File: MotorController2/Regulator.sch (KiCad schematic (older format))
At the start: 21 parts, among them U4 IFX91041EJV50, U5 TC2117-3.3V

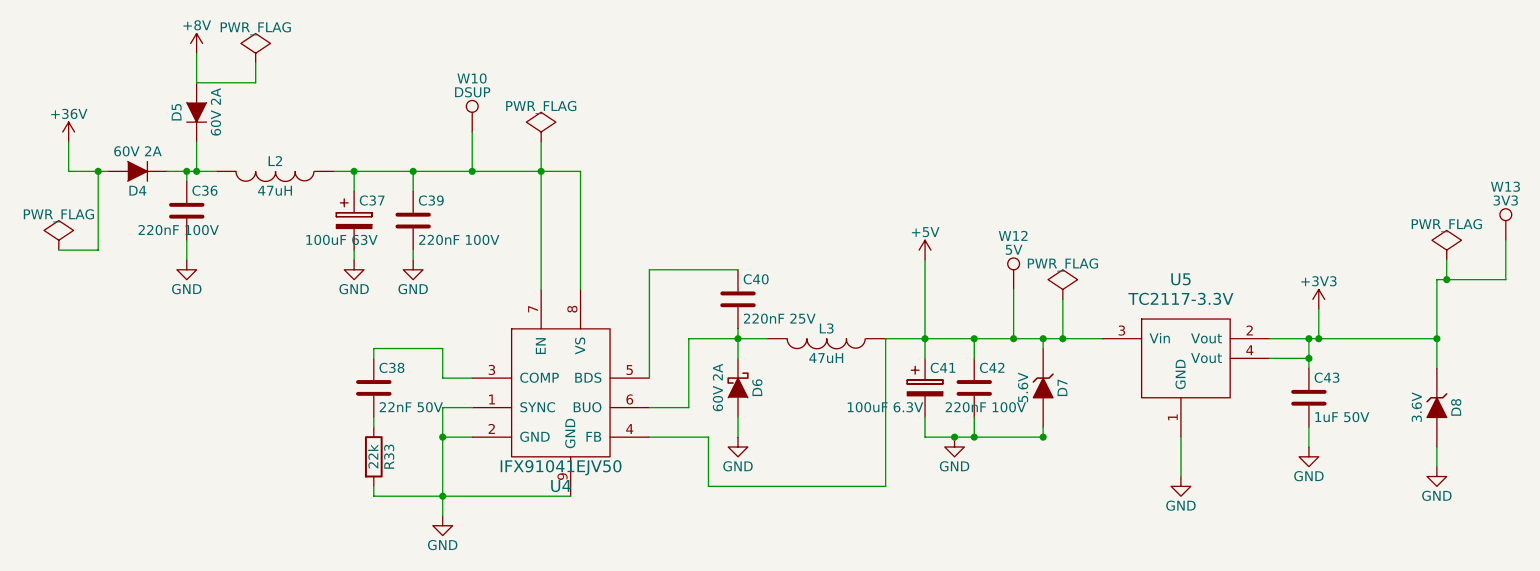
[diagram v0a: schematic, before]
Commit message: Add power off option.
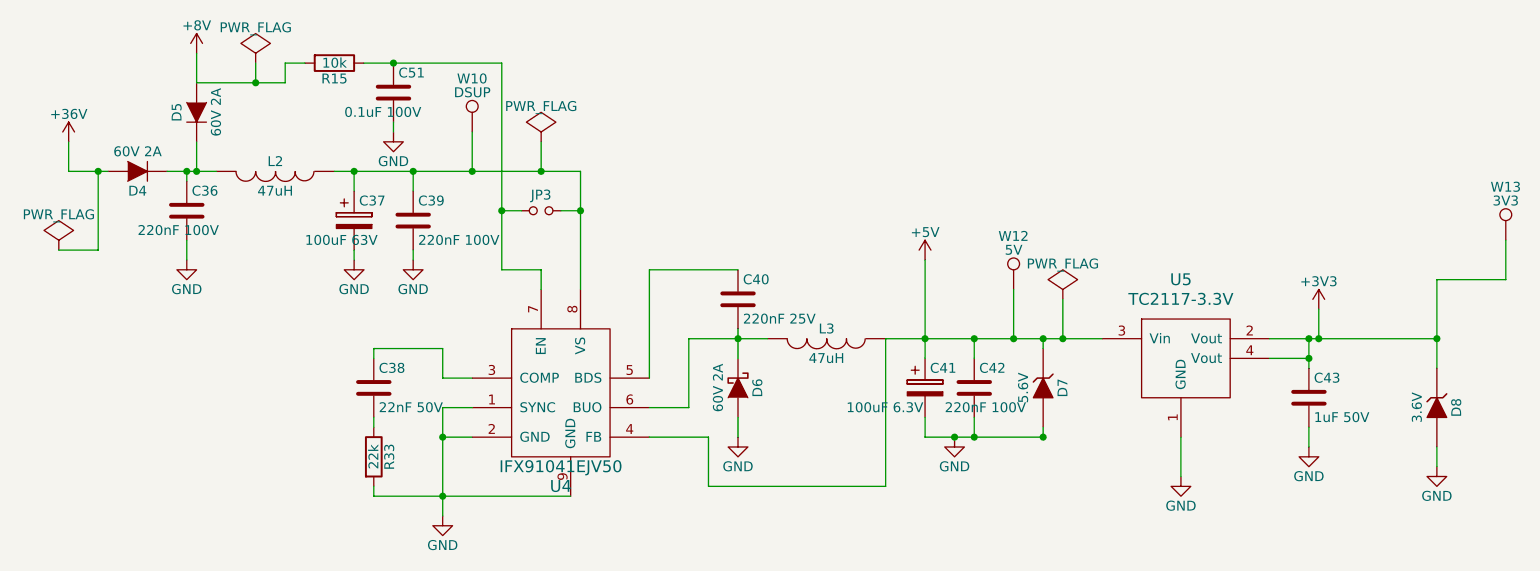
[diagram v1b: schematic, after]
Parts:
- added C51: 0.1uF 100V, Capacitors_SMD:C_0805_HandSoldering, symbol C
- added JP3: Jumper_NO_Small, Resistors_SMD:R_0805_HandSoldering, symbol Jumper_NO_Small
- added R15: 10k, Resistors_SMD:R_0805_HandSoldering, symbol R
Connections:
- net +8V: now also R15.2
- net GND: now also C51.2
- net at C37.1, C39.1, L2.1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: now also JP3.2; no longer U4.7 (EN)
- new net: C51.1, JP3.1, R15.1, U4.7 (EN)
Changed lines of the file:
@@
-EESchema Schematic File Version 3
+EESchema Schematic File Version 2
 LIBS:BMC2-rescue
 LIBS:power
@@
 LIBS:MIC2009A-1YM6TR
 LIBS:BMC2-cache
-EELAYER 26 0
+EELAYER 25 0
 EELAYER END
 $Descr A4 11693 8268
@@
 $EndDescr
 $Comp
-L GND #PWR077
+L GND #PWR053
 U 1 1 585F6F4B
 P 2850 3350
-F 0 "#PWR077" H 2850 3100 50  0001 C CNN
+F 0 "#PWR053" H 2850 3100 50  0001 C CNN
 F 1 "GND" H 2850 3200 50  0000 C CNN
 F 2 "" H 2850 3350 50  0000 C CNN
@@
 	2850 2650 3000 2650
 $Comp
-L +36V #PWR078
+L +36V #PWR054
 U 1 1 585F700E
 P 950 1450
-F 0 "#PWR078" H 950 1300 50  0001 C CNN
+F 0 "#PWR054" H 950 1300 50  0001 C CNN
 F 1 "+36V" H 950 1590 50  0000 C CNN
 F 2 "" H 950 1450 50  0000 C CNN
@@
 	4100 2800 4100 2450
 $Comp
-L GND #PWR079
+L GND #PWR055
 U 1 1 585F787D
 P 4350 2950
-F 0 "#PWR079" H 4350 2700 50  0001 C CNN
+F 0 "#PWR055" H 4350 2700 50  0001 C CNN
 F 1 "GND" H 4350 2800 50  0000 C CNN
 F 2 "" H 4350 2950 50  0000 C CNN
@@
 	4350 2950 4350 2850
 $Comp
-L GND #PWR080
+L GND #PWR056
 U 1 1 585F7983
 P 5450 2950
-F 0 "#PWR080" H 5450 2700 50  0001 C CNN
+F 0 "#PWR056" H 5450 2700 50  0001 C CNN
 F 1 "GND" H 5450 2800 50  0000 C CNN
 F 2 "" H 5450 2950 50  0000 C CNN
@@
 Connection ~ 2700 1600
 $Comp
-L GND #PWR081
+L GND #PWR057
 U 1 1 585F7C36
 P 1550 2050
-F 0 "#PWR081" H 1550 1800 50  0001 C CNN
+F 0 "#PWR057" H 1550 1800 50  0001 C CNN
 F 1 "GND" H 1550 1900 50  0000 C CNN
 F 2 "" H 1550 2050 50  0000 C CNN
@@
 $EndComp
 $Comp
-L GND #PWR082
+L GND #PWR058
 U 1 1 585F7C68
 P 2400 2050
-F 0 "#PWR082" H 2400 1800 50  0001 C CNN
+F 0 "#PWR058" H 2400 1800 50  0001 C CNN
 F 1 "GND" H 2400 1900 50  0000 C CNN
 F 2 "" H 2400 2050 50  0000 C CNN
@@
 $EndComp
 $Comp
-L GND #PWR083
+L GND #PWR059
 U 1 1 585F7C9A
 P 2700 2050
-F 0 "#PWR083" H 2700 1800 50  0001 C CNN
+F 0 "#PWR059" H 2700 1800 50  0001 C CNN
 F 1 "GND" H 2700 1900 50  0000 C CNN
 F 2 "" H 2700 2050 50  0000 C CNN
@@
 	2700 2050 2700 2000
 Wire Wire Line
-	3350 1450 3350 2200
+	3350 1450 3350 1600
 Connection ~ 3350 1600
 $Comp
@@
 $EndComp
 $Comp
-L +5V #PWR084
+L +5V #PWR060
 U 1 1 586591BB
 P 5300 2050
-F 0 "#PWR084" H 5300 1900 50  0001 C CNN
+F 0 "#PWR060" H 5300 1900 50  0001 C CNN
 F 1 "+5V" H 5300 2190 50  0000 C CNN
 F 2 "" H 5300 2050 50  0000 C CNN
@@
 Connection ~ 1600 1600
 $Comp
-L +8V #PWR085
+L +8V #PWR061
 U 1 1 5865931B
 P 1600 1000
-F 0 "#PWR085" H 1600 850 50  0001 C CNN
+F 0 "#PWR061" H 1600 850 50  0001 C CNN
 F 1 "+8V" H 1600 1140 50  0000 C CNN
 F 2 "" H 1600 1000 50  0000 C CNN
@@
 	1600 1000 1600 1150
 $Comp
-L GND #PWR086
+L GND #PWR062
 U 1 1 586595C6
 P 6600 3150
-F 0 "#PWR086" H 6600 2900 50  0001 C CNN
+F 0 "#PWR062" H 6600 2900 50  0001 C CNN
 F 1 "GND" H 6600 3000 50  0000 C CNN
 F 2 "" H 6600 3150 50  0000 C CNN
@@
 	6600 3150 6600 2950
 $Comp
-L +3V3 #PWR087
+L +3V3 #PWR063
 U 1 1 58659680
 P 7300 2300
-F 0 "#PWR087" H 7300 2150 50  0001 C CNN
+F 0 "#PWR063" H 7300 2150 50  0001 C CNN
 F 1 "+3V3" H 7300 2440 50  0000 C CNN
 F 2 "" H 7300 2300 50  0000 C CNN
@@
 $EndComp
 $Comp
-L GND #PWR088
+L GND #PWR064
 U 1 1 586598C9
 P 7250 3000
-F 0 "#PWR088" H 7250 2750 50  0001 C CNN
+F 0 "#PWR064" H 7250 2750 50  0001 C CNN
 F 1 "GND" H 7250 2850 50  0000 C CNN
 F 2 "" H 7250 3000 50  0000 C CNN
@@
 	7250 3000 7250 2900
 Wire Wire Line
-	7250 2600 7250 2450
+	7250 2450 7250 2600
 Connection ~ 7250 2450
 $Comp
@@
 	5300 2950 5900 2950
 $Comp
-L GND #PWR089
+L GND #PWR065
 U 1 1 5865A3E7
 P 7900 3100
-F 0 "#PWR089" H 7900 2850 50  0001 C CNN
+F 0 "#PWR065" H 7900 2850 50  0001 C CNN
 F 1 "GND" H 7900 2950 50  0000 C CNN
 F 2 "" H 7900 3100 50  0000 C CNN
@@
 Connection ~ 3000 1600
 $Comp
-L PWR_FLAG #FLG092
+L PWR_FLAG #FLG066
 U 1 1 5874647E
 P 6000 2250
-F 0 "#FLG092" H 6000 2345 50  0001 C CNN
+F 0 "#FLG066" H 6000 2345 50  0001 C CNN
 F 1 "PWR_FLAG" H 6000 2430 50  0000 C CNN
 F 2 "" H 6000 2250 50  0000 C CNN
@@
 Connection ~ 6000 2450
 $Comp
-L PWR_FLAG #FLG093
-U 1 1 58746589
-P 7950 2050
-F 0 "#FLG093" H 7950 2145 50  0001 C CNN
-F 1 "PWR_FLAG" H 7950 2230 50  0000 C CNN
-F 2 "" H 7950 2050 50  0000 C CNN
-F 3 "" H 7950 2050 50  0000 C CNN
-	1    7950 2050
-	1    0    0    -1
-$EndComp
-Wire Wire Line
-	7950 2050 7950 2150
-Connection ~ 7950 2150
-$Comp
-L PWR_FLAG #FLG094
+L PWR_FLAG #FLG067
 U 1 1 58746947
 P 1900 1050
-F 0 "#FLG094" H 1900 1145 50  0001 C CNN
+F 0 "#FLG067" H 1900 1145 50  0001 C CNN
 F 1 "PWR_FLAG" H 1900 1230 50  0000 C CNN
 F 2 "" H 1900 1050 50  0000 C CNN
@@
 	1900 1050 1900 1150
 Wire Wire Line
-	1900 1150 1600 1150
-$Comp
-L PWR_FLAG #FLG095
+	1600 1150 2050 1150
+$Comp
+L PWR_FLAG #FLG068
 U 1 1 58746A06
 P 900 2000
-F 0 "#FLG095" H 900 2095 50  0001 C CNN
+F 0 "#FLG068" H 900 2095 50  0001 C CNN
 F 1 "PWR_FLAG" H 900 2180 50  0000 C CNN
 F 2 "" H 900 2000 50  0000 C CNN
@@
 Connection ~ 1100 1600
 $Comp
-L PWR_FLAG #FLG096
+L PWR_FLAG #FLG069
 U 1 1 58764812
 P 3350 1450
-F 0 "#FLG096" H 3350 1545 50  0001 C CNN
+F 0 "#FLG069" H 3350 1545 50  0001 C CNN
 F 1 "PWR_FLAG" H 3350 1630 50  0000 C CNN
 F 2 "" H 3350 1450 50  0000 C CNN
@@
 $EndComp
 Connection ~ 7250 2550
-Wire Wire Line
-	7900 2150 8250 2150
 $Comp
 L TC2117-3.3V U5
@@
 Wire Wire Line
 	7050 2550 7250 2550
+$Comp
+L R R15
+U 1 1 59C4B75A
+P 2300 1050
+F 0 "R15" V 2380 1050 50  0000 C CNN
+F 1 "10k" V 2300 1050 50  0000 C CNN
+F 2 "Resistors_SMD:R_0805_HandSoldering" V 2230 1050 50  0001 C CNN
+F 3 "" H 2300 1050 50  0000 C CNN
+	1    2300 1050
+	0    1    1    0
+$EndComp
+$Comp
+L C C51
+U 1 1 59C4B98C
+P 2600 1200
+F 0 "C51" H 2625 1300 50  0000 L CNN
+F 1 "0.1uF 100V" H 2350 1100 50  0000 L CNN
+F 2 "Capacitors_SMD:C_0805_HandSoldering" H 2638 1050 50  0001 C CNN
+F 3 "" H 2600 1200 50  0000 C CNN
+F 4 "1856615" H 2600 1200 60  0001 C CNN "Farnell"
+	1    2600 1200
+	1    0    0    -1
+$EndComp
+Wire Wire Line
+	2050 1150 2050 1050
+Wire Wire Line
+	2050 1050 2150 1050
+Connection ~ 1900 1150
+Wire Wire Line
+	2450 1050 3150 1050
+$Comp
+L GND #PWR070
+U 1 1 59C4BBA7
+P 2600 1400
+F 0 "#PWR070" H 2600 1150 50  0001 C CNN
+F 1 "GND" H 2600 1250 50  0000 C CNN
+F 2 "" H 2600 1400 50  0000 C CNN
+F 3 "" H 2600 1400 50  0000 C CNN
+	1    2600 1400
+	1    0    0    -1
+$EndComp
+Wire Wire Line
+	2600 1400 2600 1350
+Wire Wire Line
+	3150 1050 3150 2100
+Wire Wire Line
+	3150 2100 3350 2100
+Wire Wire Line
+	3350 2100 3350 2200
+Connection ~ 2600 1050
+$Comp
+L Jumper_NO_Small JP3
+U 1 1 59C4C18F
+P 3350 1800
+F 0 "JP3" H 3350 1880 50  0000 C CNN
+F 1 "Jumper_NO_Small" H 3360 1740 50  0001 C CNN
+F 2 "Resistors_SMD:R_0805_HandSoldering" H 3350 1800 50  0001 C CNN
+F 3 "" H 3350 1800 50  0000 C CNN
+	1    3350 1800
+	1    0    0    -1
+$EndComp
+Wire Wire Line
+	3450 1800 3550 1800
+Connection ~ 3550 1800
+Wire Wire Line
+	3250 1800 3150 1800
+Connection ~ 3150 1800
+Wire Wire Line
+	7900 2150 8250 2150
 $EndSCHEMATC

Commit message: Updates for parts list.
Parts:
- C36, C40, C42: Price (none) -> 0.205
- C37: Price (none) -> 0.43
- C38: Farnell 2581093 -> 1414682; Price (none) -> 0.0246
- C41: Price (none) -> 0.138
- C51: Farnell 1856615 -> 1650862; Notes (none) -> +- 10%; Price (none) -> 0.116
- D7: value 5.6V -> 5.6V Zener; Farnell 1431292 -> 1459122; Mouser (none) -> 863-SZMMSZ5V6T1G; OldPart (none) -> MMSZ5V6T1G; Part MMSZ5V6T1G -> MMSZ4690T1G; Price (none) -> 0.16; Supplier (none) -> ?
- D8: value 3.6V -> 3.6V Zener; Farnell 1651592 -> 1700854; Part MMSZ4685T1G -> MMSZ5227B; PartPrevious (none) -> MMSZ4685T1G; Price (none) -> 0.155
- JP3: Supplier (none) -> None
- L2: Farnell (none) -> 2345091; Price (none) -> 0.765
- R15: value 10k -> 10K
- R33: Farnell (none) -> 9238646; Price (none) -> 0.01
- U4: Farnell (none) -> 2432504; Price (none) -> 1.10
- U5: Farnell (none) -> 1605581; Price  (none) -> 0.669
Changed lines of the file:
@@
-EESchema Schematic File Version 2
+EESchema Schematic File Version 3
 LIBS:BMC2-rescue
 LIBS:power
 LIBS:device
-LIBS:transistors
-LIBS:conn
 LIBS:linear
 LIBS:regul
-LIBS:74xx
-LIBS:cmos4000
 LIBS:adc-dac
 LIBS:memory
@@
 LIBS:digital-audio
 LIBS:philips
-LIBS:display
 LIBS:cypress
 LIBS:siliconi
@@
 LIBS:atmel
 LIBS:contrib
-LIBS:valves
-LIBS:stm32
 LIBS:Power_Management
 LIBS:motor_drivers
@@
 LIBS:MIC2009A-1YM6TR
 LIBS:BMC2-cache
-EELAYER 25 0
+EELAYER 26 0
 EELAYER END
 $Descr A4 11693 8268
@@
 F 2 "Capacitors_SMD:C_0805_HandSoldering" H 2538 2550 50  0001 C CNN
 F 3 "" H 2500 2700 50  0000 C CNN
-F 4 "2581093" H 2500 2700 60  0001 C CNN "Farnell"
+F 4 "1414682" H 2500 2700 60  0001 C CNN "Farnell"
 F 5 "6V" H 2500 2700 60  0001 C CNN "Notes"
+F 6 "0.0246" H 2500 2700 60  0001 C CNN "Price"
 	1    2500 2700
 	1    0    0    -1
@@
 F 2 "Resistors_SMD:R_0805_HandSoldering" V 2430 3050 50  0001 C CNN
 F 3 "" H 2500 3050 50  0000 C CNN
+F 4 "0.01" V 2500 3050 60  0001 C CNN "Price"
+F 5 "9238646" V 2500 3050 60  0001 C CNN "Farnell"
 	1    2500 3050
 	1    0    0    -1
@@
 F 3 "" H 1550 1800 50  0000 C CNN
 F 4 "1856615" H 1550 1800 60  0001 C CNN "Farnell"
+F 5 "0.205" H 1550 1800 60  0001 C CNN "Price"
 	1    1550 1800
 	1    0    0    -1
@@
 F 3 "" H 2000 1600 50  0000 C CNN
 F 4 "http://uk.farnell.com/tdk/clf7045t-470m/inductor-47uh-1-3a-20-smd/dp/2345091" V 2000 1600 60  0001 C CNN "Order"
+F 5 "2345091" V 2000 1600 60  0001 C CNN "Farnell"
+F 6 "0.765" V 2000 1600 60  0001 C CNN "Price"
 	1    2000 1600
 	0    1    1    0
@@
 F 3 "" H 2400 1850 50  0000 C CNN
 F 4 "9696040" H 2400 1850 60  0001 C CNN "Farnell"
+F 5 "0.43" H 2400 1850 60  0001 C CNN "Price"
 	1    2400 1850
 	1    0    0    -1
@@
 F 4 "6V" H 4350 2250 60  0001 C CNN "Notes"
 F 5 "1856615" H 4350 2250 60  0001 C CNN "Farnell"
+F 6 "0.205" H 4350 2250 60  0001 C CNN "Price"
 	1    4350 2250
 	1    0    0    -1
@@
 F 3 "" H 5300 2700 50  0000 C CNN
 F 4 "2611349" H 5300 2700 60  0001 C CNN "Farnell"
+F 5 "0.138" H 5300 2700 60  0001 C CNN "Price"
 	1    5300 2700
 	1    0    0    -1
@@
 F 4 "6V" H 5550 2700 60  0001 C CNN "Notes"
 F 5 "1856615" H 5550 2700 60  0001 C CNN "Farnell"
+F 6 "0.205" H 5550 2700 60  0001 C CNN "Price"
 	1    5550 2700
 	1    0    0    -1
@@
 P 5900 2700
 F 0 "D7" H 5900 2800 50  0000 C CNN
-F 1 "5.6V" H 5900 2600 50  0000 C CNN
+F 1 "5.6V Zener" H 5900 2900 50  0000 C CNN
 F 2 "Diodes_SMD:SOD-123" H 5900 2700 50  0001 C CNN
 F 3 "" H 5900 2700 50  0000 C CNN
-F 4 "MMSZ5V6T1G" H 5900 2700 60  0001 C CNN "Part"
+F 4 "MMSZ4690T1G" H 5900 2700 60  0001 C CNN "Part"
 F 5 "http://uk.farnell.com/on-semiconductor/mmsz5v6t1g/diode-zener-5-6v-0-5w/dp/1431292" H 5900 2700 60  0001 C CNN "Order"
-F 6 "1431292" H 5900 2700 60  0001 C CNN "Farnell"
+F 6 "1459122" H 5900 2700 60  0001 C CNN "Farnell"
+F 7 "863-SZMMSZ5V6T1G" H 5900 2700 60  0001 C CNN "Mouser"
+F 8 "?" H 5900 2700 60  0001 C CNN "Supplier"
+F 9 "0.16" H 5900 2700 60  0001 C CNN "Price"
+F 10 "MMSZ5V6T1G" H 5900 2700 60  0001 C CNN "OldPart"
 	1    5900 2700
 	0    1    1    0
@@
 F 3 "http://www.infineon.com/dgdl/Infineon-IFX91041-DS-v01_01-en.pdf?fileId=db3a304320d39d59012153afb91a0548" H 3450 3100 60  0001 C CNN
 F 4 "https://www.digikey.co.uk/product-detail/en/infineon-technologies/IFX91041EJ-V50/IFX91041EJ-V50INCT-ND/3300395" H 3450 3100 60  0001 C CNN "Order"
+F 5 "2432504" H 3450 3100 60  0001 C CNN "Farnell"
+F 6 "1.10" H 3450 3100 60  0001 C CNN "Price"
 	1    3450 3100
 	1    0    0    -1
@@
 P 7900 2800
 F 0 "D8" H 7900 2900 50  0000 C CNN
-F 1 "3.6V" H 7900 2700 50  0000 C CNN
+F 1 "3.6V Zener" H 7900 2700 50  0000 C CNN
 F 2 "Diodes_SMD:SOD-123" H 7900 2800 50  0001 C CNN
 F 3 "" H 7900 2800 50  0000 C CNN
 F 4 "http://uk.farnell.com/on-semiconductor/mmsz4685t1g/diode-zener-vz-3-6v/dp/1651592" H 7900 2800 60  0001 C CNN "Order"
-F 5 "MMSZ4685T1G" H 7900 2800 60  0001 C CNN "Part"
-F 6 "1651592" H 7900 2800 60  0001 C CNN "Farnell"
+F 5 "MMSZ5227B" H 7900 2800 60  0001 C CNN "Part"
+F 6 "1700854" H 7900 2800 60  0001 C CNN "Farnell"
+F 7 "MMSZ4685T1G" H 7900 2800 60  0001 C CNN "PartPrevious"
+F 8 "0.155" H 7900 2800 60  0001 C CNN "Price"
 	1    7900 2800
 	0    1    1    0
@@
 F 3 "http://www.farnell.com/datasheets/1669439.pdf?_ga=1.267823246.1808009743.1471515981" H 6600 2550 60  0001 C CNN
 F 4 "http://uk.farnell.com/microchip/tc2117-3-3vdbtr/ic-cmso-ldo-3-3v-800ma-sot223/dp/1605581" H 6600 2550 60  0001 C CNN "Order"
+F 5 "1605581" H 6600 2550 60  0001 C CNN "Farnell"
+F 6 "0.669" H 6600 2550 60  0001 C CNN "Price "
 	1    6600 2550
 	1    0    0    -1
@@
 P 2300 1050
 F 0 "R15" V 2380 1050 50  0000 C CNN
-F 1 "10k" V 2300 1050 50  0000 C CNN
+F 1 "10K" V 2300 1050 50  0000 C CNN
 F 2 "Resistors_SMD:R_0805_HandSoldering" V 2230 1050 50  0001 C CNN
 F 3 "" H 2300 1050 50  0000 C CNN
@@
 F 2 "Capacitors_SMD:C_0805_HandSoldering" H 2638 1050 50  0001 C CNN
 F 3 "" H 2600 1200 50  0000 C CNN
-F 4 "1856615" H 2600 1200 60  0001 C CNN "Farnell"
+F 4 "1650862" H 2600 1200 60  0001 C CNN "Farnell"
+F 5 "+- 10%" H 2600 1200 60  0001 C CNN "Notes"
+F 6 "0.116" H 2600 1200 60  0001 C CNN "Price"
 	1    2600 1200
 	1    0    0    -1
@@
 F 2 "Resistors_SMD:R_0805_HandSoldering" H 3350 1800 50  0001 C CNN
 F 3 "" H 3350 1800 50  0000 C CNN
+F 4 "None" H 3350 1800 60  0001 C CNN "Supplier"
 	1    3350 1800
 	1    0    0    -1

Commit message: Add some annotations.
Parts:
- C51: value 0.1uF 100V -> 0.1uF 50V; Farnell 1650862 -> (none)
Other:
- note added: "When JP3 is not fitted the external +8V line acts as \na master power switch for all the boards."
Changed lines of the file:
@@
-EESchema Schematic File Version 3
+EESchema Schematic File Version 2
 LIBS:BMC2-rescue
 LIBS:power
 LIBS:device
+LIBS:transistors
+LIBS:conn
 LIBS:linear
 LIBS:regul
+LIBS:74xx
+LIBS:cmos4000
 LIBS:adc-dac
 LIBS:memory
@@
 LIBS:digital-audio
 LIBS:philips
+LIBS:display
 LIBS:cypress
 LIBS:siliconi
@@
 LIBS:atmel
 LIBS:contrib
+LIBS:valves
+LIBS:stm32
 LIBS:Power_Management
 LIBS:motor_drivers
@@
 LIBS:MIC2009A-1YM6TR
 LIBS:BMC2-cache
-EELAYER 26 0
+EELAYER 25 0
 EELAYER END
 $Descr A4 11693 8268
@@
 P 2600 1200
 F 0 "C51" H 2625 1300 50  0000 L CNN
-F 1 "0.1uF 100V" H 2350 1100 50  0000 L CNN
+F 1 "0.1uF 50V" H 2350 1100 50  0000 L CNN
 F 2 "Capacitors_SMD:C_0805_HandSoldering" H 2638 1050 50  0001 C CNN
 F 3 "" H 2600 1200 50  0000 C CNN
-F 4 "1650862" H 2600 1200 60  0001 C CNN "Farnell"
-F 5 "+- 10%" H 2600 1200 60  0001 C CNN "Notes"
-F 6 "0.116" H 2600 1200 60  0001 C CNN "Price"
+F 4 "+- 10%" H 2600 1200 60  0001 C CNN "Notes"
+F 5 "0.116" H 2600 1200 60  0001 C CNN "Price"
 	1    2600 1200
 	1    0    0    -1
@@
 Wire Wire Line
 	7900 2150 8250 2150
+Text Notes 3500 1550 0    60   ~ 0
+When JP3 is not fitted the external +8V line acts as \na master power switch for all the boards.
 $EndSCHEMATC
